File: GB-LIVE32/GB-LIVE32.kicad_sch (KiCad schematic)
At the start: 39 parts

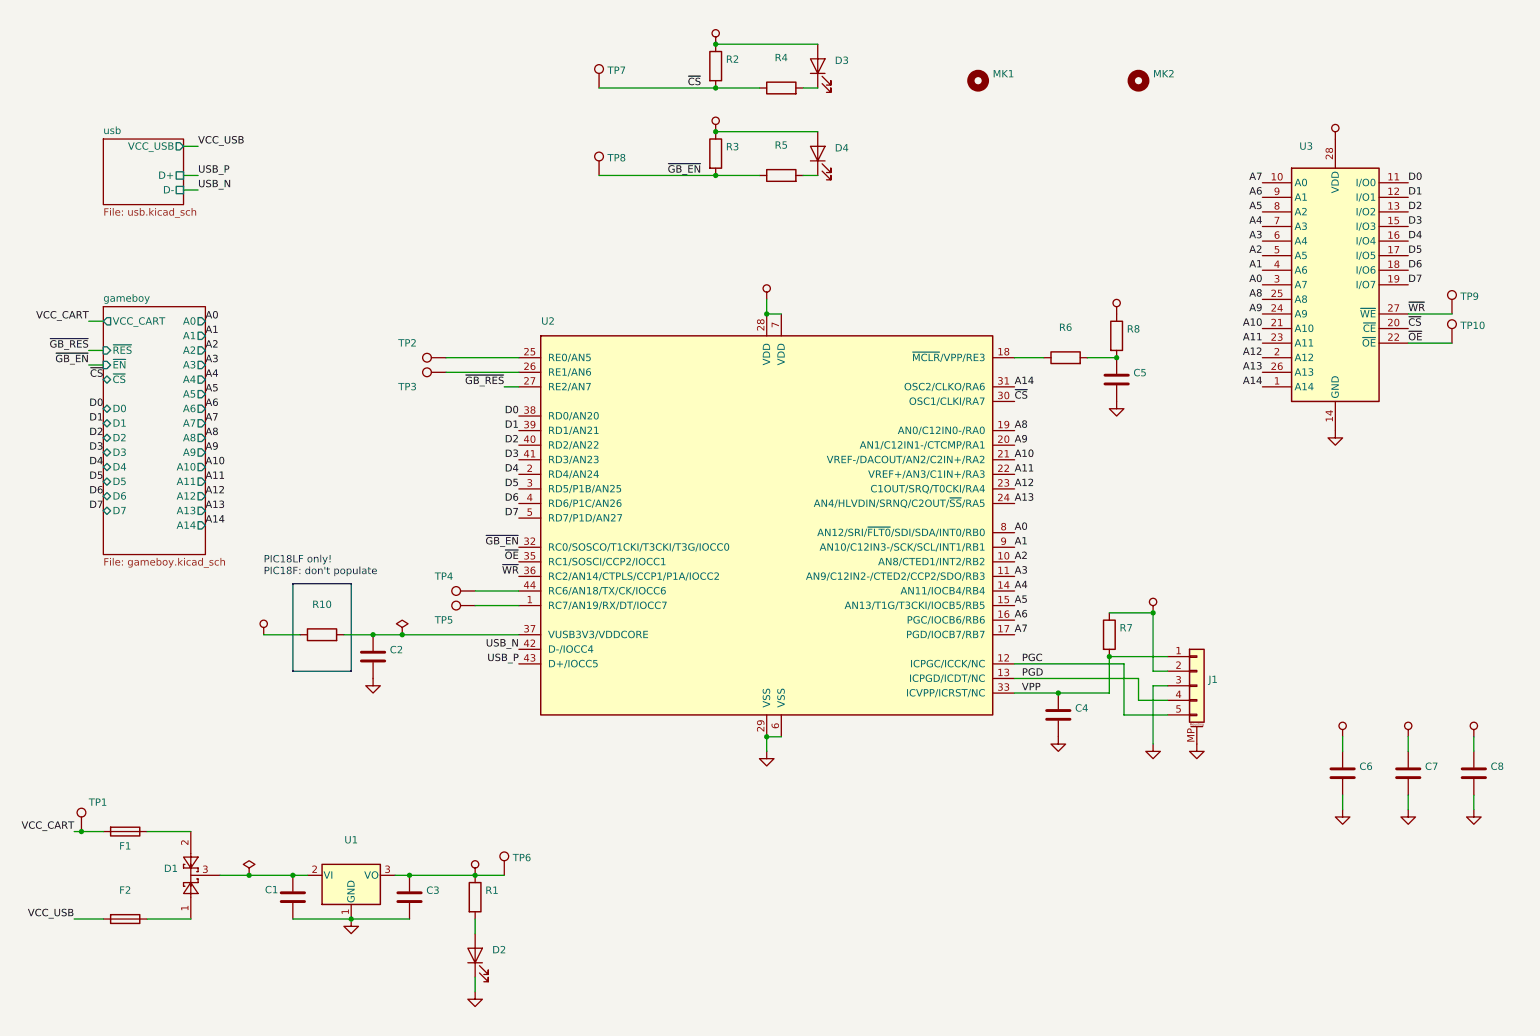
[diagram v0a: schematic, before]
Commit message: Upgrade projects to KiCad 7
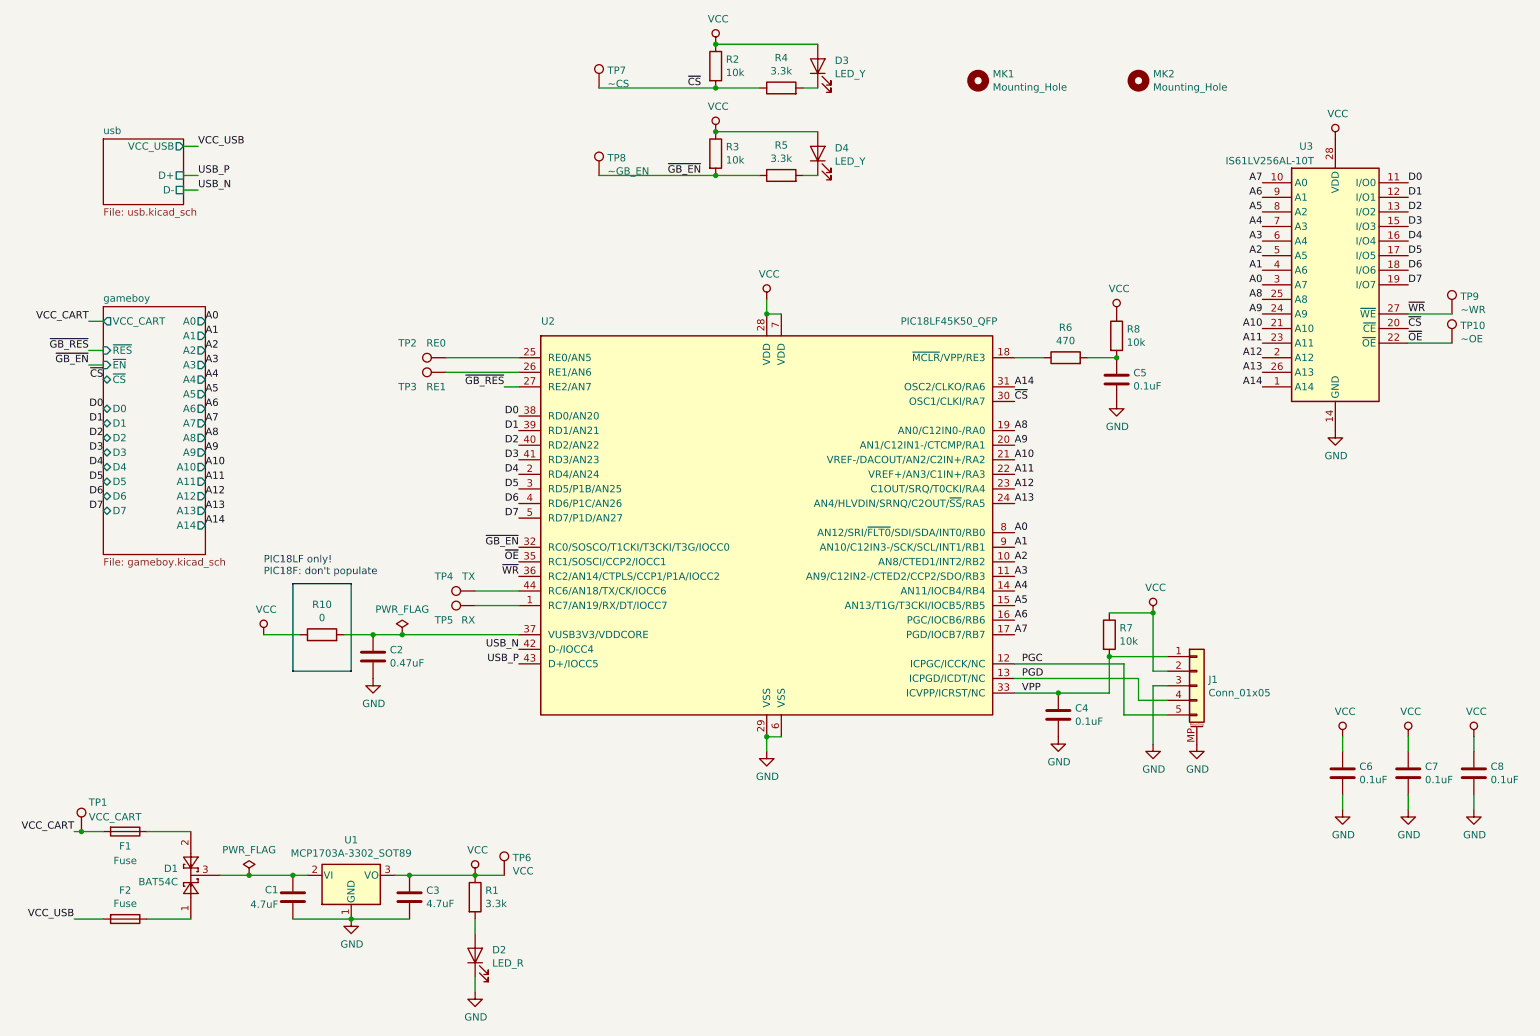
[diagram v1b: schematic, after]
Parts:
- C1, C3: value (none) -> 4.7uF; footprint (none) -> Capacitor_SMD:C_0805_2012Metric
- C2: value (none) -> 0.47uF; footprint (none) -> Capacitor_SMD:C_0603_1608Metric
- C4, C5, C6, C7, C8: value (none) -> 0.1uF; footprint (none) -> Capacitor_SMD:C_0603_1608Metric
- D1: value (none) -> BAT54C; footprint (none) -> Package_TO_SOT_SMD:SOT-23
- D2: value (none) -> LED_R; footprint (none) -> LED_SMD:LED_0603_1608Metric
- D3, D4: value (none) -> LED_Y; footprint (none) -> LED_SMD:LED_0603_1608Metric
- F1, F2: value (none) -> Fuse; footprint (none) -> Fuse:Fuse_0603_1608Metric
- J1: value (none) -> Conn_01x05; footprint (none) -> Connector_Molex:Molex_Pico-Lock_504050-0591_1x05-1MP_P1.50mm_Horizontal
- MK1: value (none) -> Mounting_Hole; footprint (none) -> Gekkio_MountingHole:MountingHole_7.2mm
- MK2: value (none) -> Mounting_Hole; footprint (none) -> Gekkio_MountingHole:MountingHole_2.3mm
- R1, R4, R5: value (none) -> 3.3k; footprint (none) -> Resistor_SMD:R_0603_1608Metric
- R10: value (none) -> 0; footprint (none) -> Resistor_SMD:R_0603_1608Metric
- R2, R3, R7, R8: value (none) -> 10k; footprint (none) -> Resistor_SMD:R_0603_1608Metric
- R6: value (none) -> 470; footprint (none) -> Resistor_SMD:R_0603_1608Metric
- TP1: value (none) -> VCC_CART; footprint (none) -> TestPoint:TestPoint_Pad_D1.0mm
- TP10: value (none) -> ~OE; footprint (none) -> TestPoint:TestPoint_Pad_D1.0mm
- TP2: value (none) -> RE0; footprint (none) -> TestPoint:TestPoint_Pad_D1.0mm
- TP3: value (none) -> RE1; footprint (none) -> TestPoint:TestPoint_Pad_D1.0mm
- TP4: value (none) -> TX; footprint (none) -> TestPoint:TestPoint_Pad_D1.0mm
- TP5: value (none) -> RX; footprint (none) -> TestPoint:TestPoint_Pad_D1.0mm
- TP6: value (none) -> VCC; footprint (none) -> TestPoint:TestPoint_Pad_D1.0mm
- TP7: value (none) -> ~CS; footprint (none) -> TestPoint:TestPoint_Pad_D1.0mm
- TP8: value (none) -> ~GB_EN; footprint (none) -> TestPoint:TestPoint_Pad_D1.0mm
- TP9: value (none) -> ~WR; footprint (none) -> TestPoint:TestPoint_Pad_D1.0mm
- U1: value (none) -> MCP1703A-3302_SOT89; footprint (none) -> Package_TO_SOT_SMD:SOT-89-3
- U2: value (none) -> PIC18LF45K50_QFP; footprint (none) -> Package_QFP:TQFP-44_10x10mm_P0.8mm
- U3: value (none) -> IS61LV256AL-10T; footprint (none) -> Gekkio_Package_SO:TSOP-I-28_11.8x8mm_P0.55mm_Pin1Middle
